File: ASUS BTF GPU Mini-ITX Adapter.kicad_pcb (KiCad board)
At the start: 2 copper layers, 38 x 25 mm, 2 parts

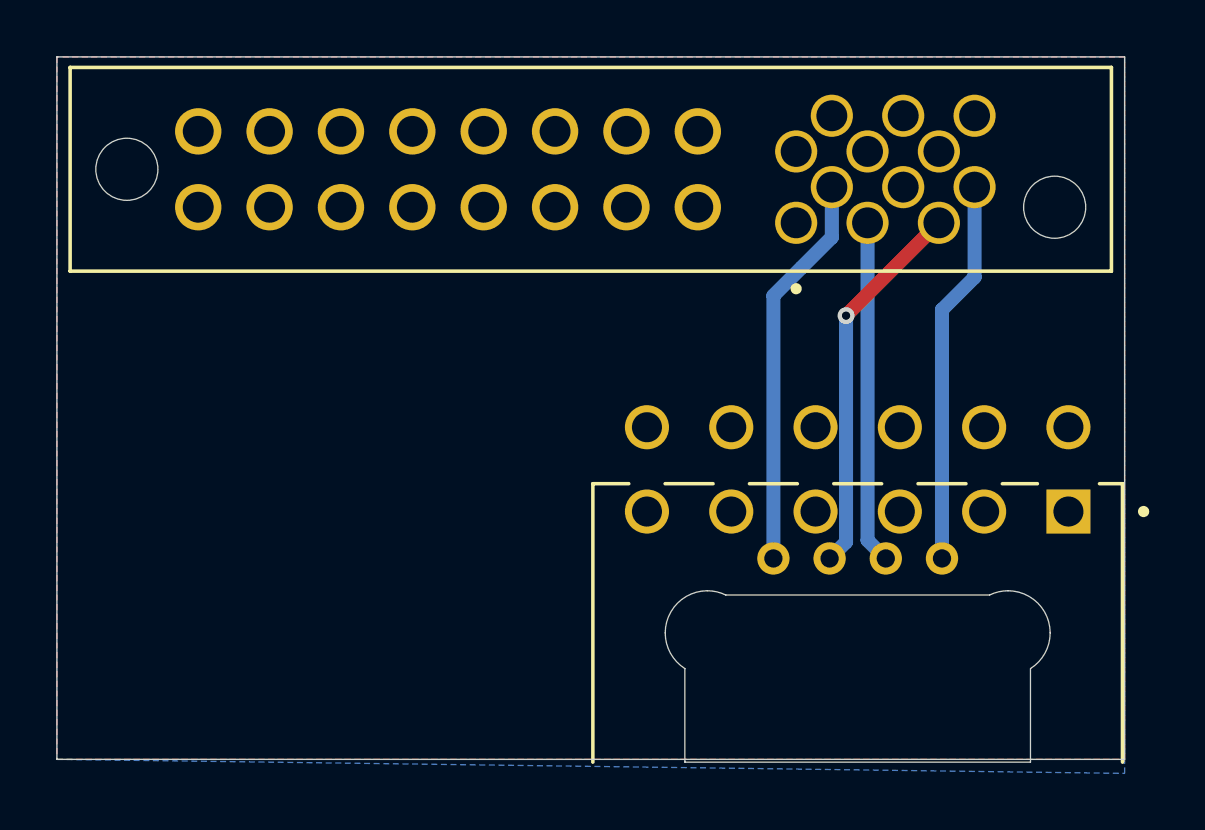
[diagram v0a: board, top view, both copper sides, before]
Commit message: updated sensor line layout
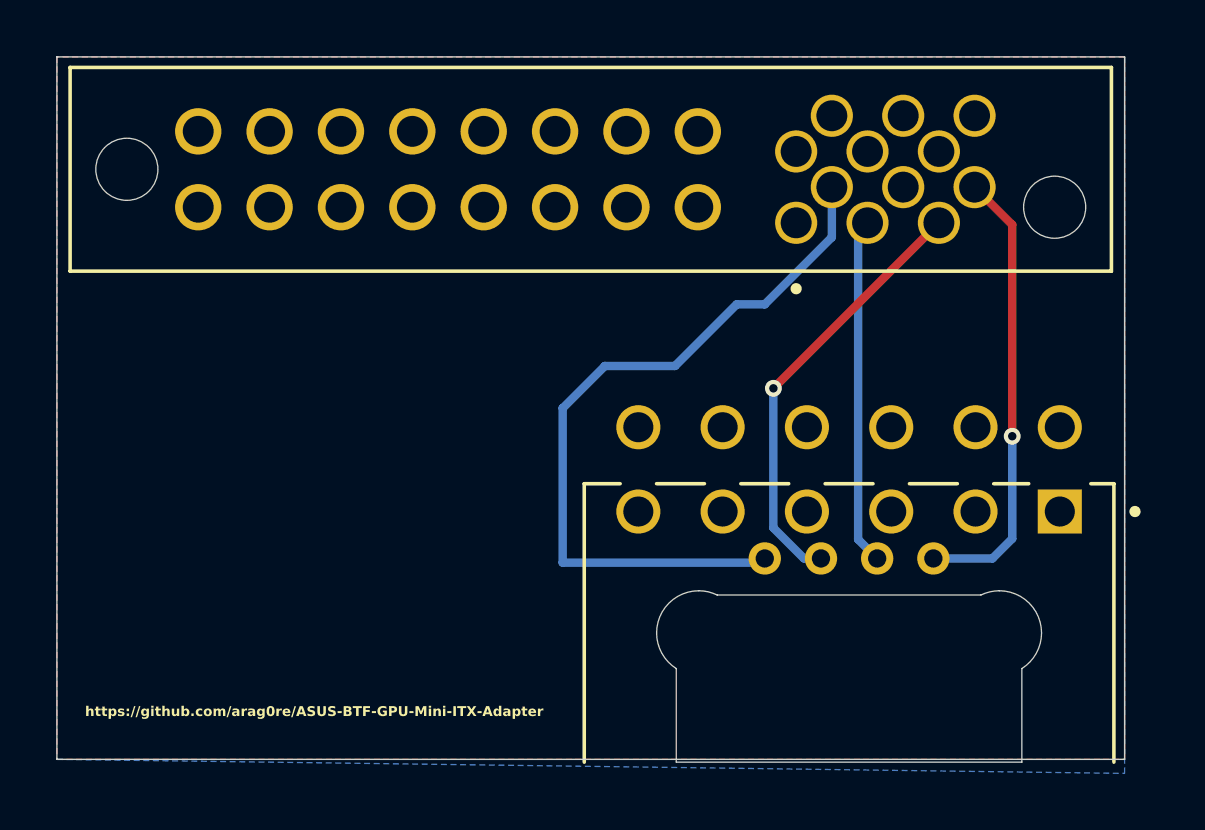
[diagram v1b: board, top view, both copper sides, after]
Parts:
- moved REF** 0.31 mm to (190.7, 120.5)
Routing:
- net SENSE1: track 14.1 -> 26.9 mm
- net CARD_PWR_STABLE: track 13.7 -> 15.9 mm, vias 0 -> 1
- net SENSE0: track 13.6 -> 15.4 mm
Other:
- board text added: "https://github.com/arag0re/ASUS-BTF-GPU-Mini-ITX-Adapter"
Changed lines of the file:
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@@
 			(outputformat 1)
 			(mirror no)
-			(drillshape 1)
+			(drillshape 0)
 			(scaleselection 1)
-			(outputdirectory "")
+			(outputdirectory "Gerbers/")
 		)
 	)
@@
 	(footprint "ASUS BTF GPU Mini-ITX Adapter:AMPHENOL_10160920-1240100LF"
 		(layer "F.Cu")
-		(at 191 120.5)
+		(at 190.69325 120.5)
 		(property "Reference" "REF**"
 			(at -6.325 -10.635 0)
@@
 		(layer "Edge.Cuts")
 	)
-	(segment
-		(start 188 108.5)
-		(end 189 107.5)
-		(width 0.5)
+	(gr_text "https://github.com/arag0re/ASUS-BTF-GPU-Mini-ITX-Adapter"
+		(at 163.5 123.5 0)
+		(layer "F.SilkS")
+		(effects
+			(font
+				(size 0.35 0.35)
+				(thickness 0.075)
+				(bold yes)
+			)
+			(justify left bottom)
+		)
+	)
+	(segment
+		(start 187.85 118)
+		(end 180.5 118)
+		(width 0.3)
 		(layer "B.Cu")
 		(net 3)
 	)
 	(segment
-		(start 188 117.85)
-		(end 188 108.5)
-		(width 0.5)
+		(start 182 111)
+		(end 184.5 111)
+		(width 0.3)
+		(layer "B.Cu")
+		(net 3)
+	)
+	(segment
+		(start 187.69325 108.80675)
+		(end 190.08 106.42)
+		(width 0.3)
 		(layer "B.Cu")
 		(net 3)
@@
 		(start 190.08 106.42)
 		(end 190.08 104.635)
-		(width 0.5)
+		(width 0.3)
 		(layer "B.Cu")
 		(net 3)
 	)
 	(segment
-		(start 189 107.5)
-		(end 190.08 106.42)
-		(width 0.5)
+		(start 188 117.85)
+		(end 187.85 118)
+		(width 0.3)
 		(layer "B.Cu")
 		(net 3)
 	)
 	(segment
-		(start 190.586 109.209)
+		(start 180.5 112.5)
+		(end 182 111)
+		(width 0.3)
+		(layer "B.Cu")
+		(net 3)
+	)
+	(segment
+		(start 180.5 118)
+		(end 180.5 112.5)
+		(width 0.3)
+		(layer "B.Cu")
+		(net 3)
+	)
+	(segment
+		(start 186.69325 108.80675)
+		(end 187.69325 108.80675)
+		(width 0.3)
+		(layer "B.Cu")
+		(net 3)
+	)
+	(segment
+		(start 184.5 111)
+		(end 186.69325 108.80675)
+		(width 0.3)
+		(layer "B.Cu")
+		(net 3)
+	)
+	(segment
+		(start 188 111.795)
 		(end 193.89 105.905)
-		(width 0.5)
+		(width 0.3)
 		(layer "F.Cu")
 		(net 4)
 	)
 	(via
-		(at 190.586 109.209)
+		(at 188 111.795)
 		(size 0.6)
 		(drill 0.3)
@@
 	)
 	(segment
-		(start 190 117.85)
-		(end 190.586 117.264)
-		(width 0.5)
+		(start 188 116.761293)
+		(end 189.088707 117.85)
+		(width 0.3)
 		(layer "B.Cu")
 		(net 4)
 	)
 	(segment
-		(start 190.586 109.209)
-		(end 190.586 117.264)
-		(width 0.5)
+		(start 189.088707 117.85)
+		(end 189.69325 117.85)
+		(width 0.3)
 		(layer "B.Cu")
 		(net 4)
 	)
 	(segment
+		(start 188 111.795)
+		(end 188 116.761293)
+		(width 0.3)
+		(layer "B.Cu")
+		(net 4)
+	)
+	(segment
+		(start 191.015693 117.172443)
+		(end 191.015693 106.239307)
+		(width 0.3)
+		(layer "B.Cu")
+		(net 5)
+	)
+	(segment
+		(start 191.015693 106.239307)
+		(end 191.35 105.905)
+		(width 0.3)
+		(layer "B.Cu")
+		(net 5)
+	)
+	(segment
+		(start 191.69325 117.85)
+		(end 191.015693 117.172443)
+		(width 0.3)
+		(layer "B.Cu")
+		(net 5)
+	)
+	(segment
 		(start 192 117.85)
-		(end 191.35 117.2)
-		(width 0.5)
+		(end 191.69325 117.85)
+		(width 0.3)
 		(layer "B.Cu")
 		(net 5)
 	)
 	(segment
-		(start 191.35 117.2)
-		(end 191.35 105.905)
-		(width 0.5)
-		(layer "B.Cu")
-		(net 5)
-	)
-	(segment
-		(start 194 117.85)
-		(end 194 109)
-		(width 0.5)
-		(layer "B.Cu")
+		(start 196.5 113.5)
+		(end 196.5 105.975)
+		(width 0.3)
+		(layer "F.Cu")
 		(net 6)
 	)
 	(segment
-		(start 195.16 107.84)
+		(start 196.5 105.975)
 		(end 195.16 104.635)
-		(width 0.5)
-		(layer "B.Cu")
+		(width 0.3)
+		(layer "F.Cu")
 		(net 6)
 	)
-	(segment
-		(start 194 109)
-		(end 195.16 107.84)
-		(width 0.5)
-		(layer "B.Cu")
+	(via
+		(at 196.5 113.5)
+		(size 0.6)
+		(drill 0.3)
+		(layers "F.Cu" "B.Cu")
 		(net 6)
+	)
+	(segment
+		(start 195.795709 117.85)
+		(end 194 117.85)
+		(width 0.3)
+		(layer "B.Cu")
+		(net 6)
+	)
+	(segment
+		(start 196.5 117.145709)
+		(end 195.795709 117.85)
+		(width 0.3)
+		(layer "B.Cu")
+		(net 6)
+	)
+	(segment
+		(start 196.5 113.5)
+		(end 196.5 117.145709)
+		(width 0.3)
+		(layer "B.Cu")
+		(net 6)
